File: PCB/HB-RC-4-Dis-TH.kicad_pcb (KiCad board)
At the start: 2 copper layers, 53 x 53 mm, 41 parts, among them J1 FTDI, J2 SHT31, J3 eInk, J4 ISP, J5 Power, Q1 IRLML6346TRBPF, SW1 T1, SW2 T2, SW3 T3, SW4 T4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

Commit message: update pcb
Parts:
- SHT31: renamed from J2; footprint Connector_PinHeader_2.00mm:PinHeader_1x04_P2.00mm_Vertical -> Connector_PinHeader_2.54mm:PinHeader_1x04_P2.54mm_Vertical
- moved SHT31 2.38 mm to (31.8, 81.3)
- moved J3 1.20 mm to (58.3, 106.5)
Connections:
- J3 pad : (no net) -> GND
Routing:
- net /RESET: track 65.1 -> 120.5 mm, vias 0 -> 3
- net Net-(C7-Pad1): track 25.5 -> 78.6 mm
- net /MOSI: track 91.1 -> 60.4 mm, vias 1 -> 3
- net GND: track 242.0 -> 264.6 mm, vias 10 -> 40
- net Net-(SW3-Pad1): track 72.4 -> 91.4 mm
- net +3V3: track 171.5 -> 189.9 mm
- net Net-(SW2-Pad1): track 24.8 -> 40.6 mm
- net /RST: track 39.7 -> 24.4 mm
- net Net-(C2-Pad1): track 22.0 -> 36.0 mm, vias 2 -> 0
- net /RX: track 66.1 -> 80.1 mm
- net /BUSY: track 41.8 -> 27.9 mm
- net /MISO: track 56.8 -> 44.2 mm
- net /DC: track 35.1 -> 25.0 mm, vias 3 -> 1
- net Net-(R1-Pad1): track 42.2 -> 51.6 mm
- net Net-(SW5-Pad1): track 74.0 -> 64.7 mm
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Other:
- outline, holes or cut-outs redrawn

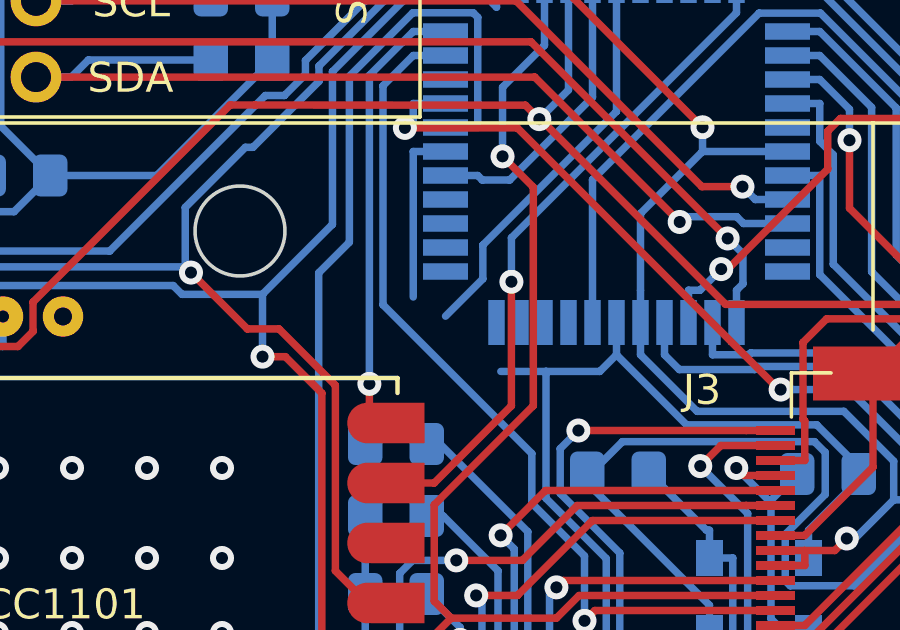
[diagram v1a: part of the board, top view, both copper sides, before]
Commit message: add via
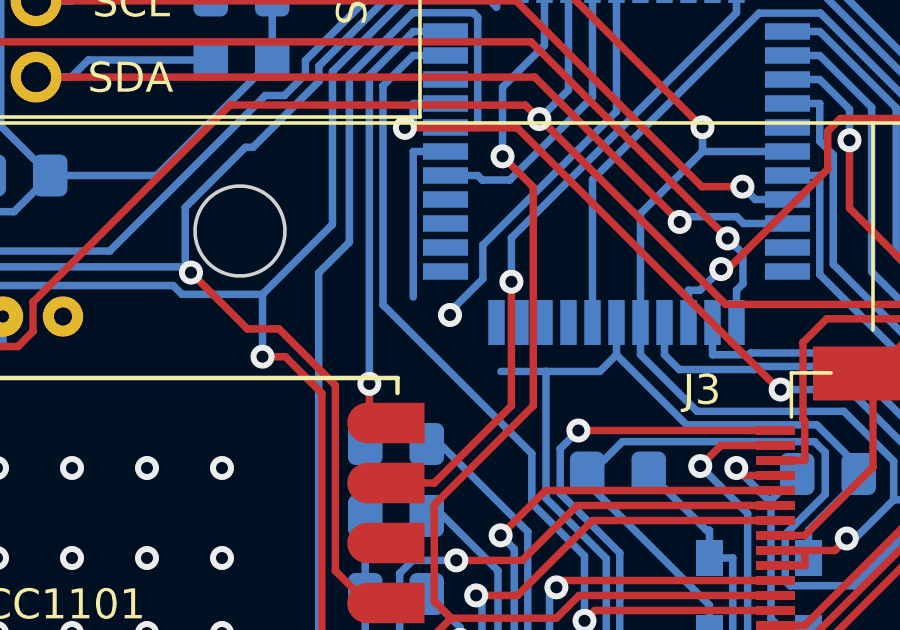
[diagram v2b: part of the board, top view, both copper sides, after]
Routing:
- net GND: vias 40 -> 41
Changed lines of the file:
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@@
     (thickness 1.6)
     (drawings 57)
-    (tracks 698)
+    (tracks 699)
     (zones 0)
     (modules 41)
@@
   (segment (start 44.3747 91.45) (end 44.3747 96.3) (width 0.25) (layer B.Cu) (net 3))
   (segment (start 45.45 91.45) (end 44.3747 91.45) (width 0.25) (layer B.Cu) (net 3))
+  (via (at 45.6 96.9) (size 0.8) (drill 0.4) (layers F.Cu B.Cu) (net 3))
   (segment (start 50.35 97.15) (end 50.35 92.39) (width 0.25) (layer B.Cu) (net 4))
   (segment (start 50.35 92.39) (end 55.9024 86.8376) (width 0.25) (layer B.Cu) (net 4))

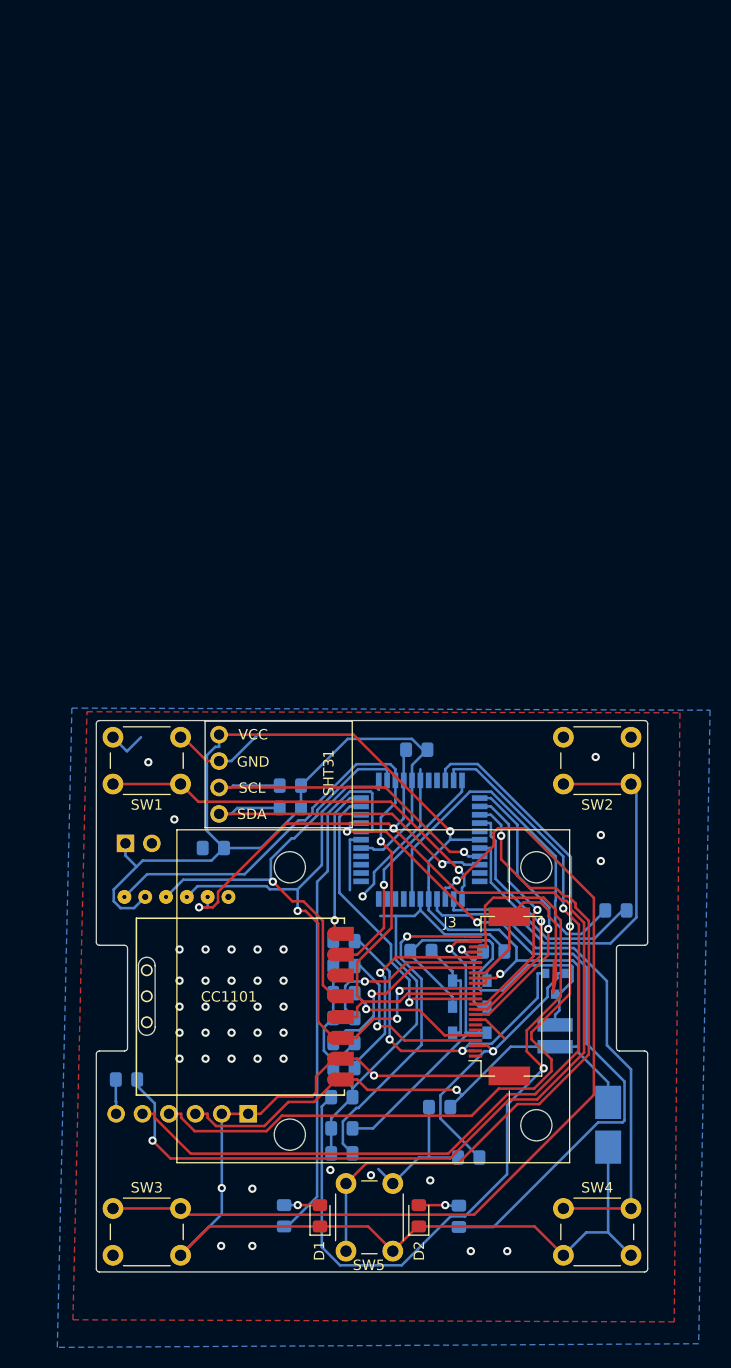
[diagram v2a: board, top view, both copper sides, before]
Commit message: update pcb v1.1 (added decoupling capacitors)
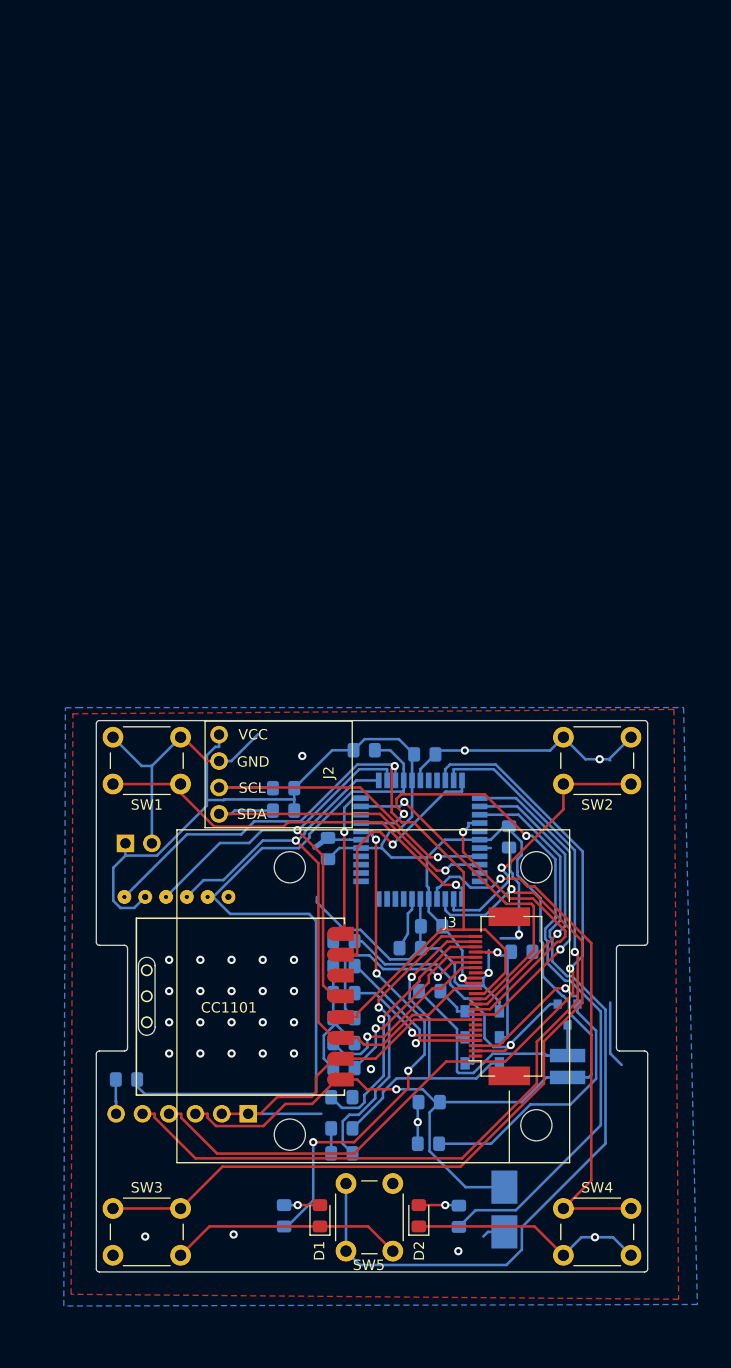
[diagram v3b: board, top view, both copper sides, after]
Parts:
- added C15: 100n, Capacitor_SMD:C_0805_2012Metric_Pad1.15x1.40mm_HandSolder, B.Cu at (51.6, 83.2)
- added C16: 100n, Capacitor_SMD:C_0805_2012Metric_Pad1.15x1.40mm_HandSolder, B.Cu at (59.7, 91.2)
- added C17: 100n, Capacitor_SMD:C_0805_2012Metric_Pad1.15x1.40mm_HandSolder, B.Cu at (52.2, 99.8)
- moved C2 20.1 mm to (50.2, 101.9)
- moved C18 12.9 mm to (59.2, 127.0)
- moved C14 11.0 mm to (42.3, 92.3), turned to 90 degrees
- moved R3 5.05 mm to (45.8, 82.8), turned to 0 degrees
- moved R8 4.10 mm to (51.9, 120.7)
- moved C11 3.94 mm to (52.0, 106.0)
- moved D3 3.18 mm to (57.1, 108.0)
- moved D4 3.18 mm to (57.1, 110.5)
- moved D5 3.18 mm to (57.1, 113.0)
- moved L1 3.18 mm to (65.3, 113.2)
- moved Q1 3.18 mm to (65.3, 108.2)
- moved C12 2.70 mm to (60.9, 102.2)
- moved C3 1.11 mm to (52.0, 116.7)
- moved R4 0.70 mm to (38.0, 86.5)
- moved R5 0.70 mm to (38.0, 88.7)
- renumbered C15 to C18, SHT31 to J2
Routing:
- net Net-(C7-Pad1): track 78.6 -> 24.8 mm
- net GND: track 264.6 -> 215.2 mm, vias 41 -> 31
- net /RESET: track 120.5 -> 74.8 mm, vias 3 -> 0
- net Net-(C2-Pad1): track 36.0 -> 5.15 mm
- net Net-(SW2-Pad1): track 40.6 -> 26.3 mm, vias 0 -> 1
- net Net-(SW5-Pad1): track 64.7 -> 78.0 mm, vias 1 -> 0
- net Net-(C11-Pad1): track 37.1 -> 24.5 mm
- net Net-(SW3-Pad1): track 91.4 -> 79.1 mm
- net /RESE: track 27.0 -> 38.8 mm
- net +3V3: track 189.9 -> 181.1 mm, vias 3 -> 2
- net /SCK: track 71.8 -> 79.0 mm
- net /PREVGL: track 28.4 -> 35.2 mm
- net /RST: track 24.4 -> 29.1 mm
- net /DC: track 25.0 -> 28.7 mm
- net /CC1101_GDO0: track 23.1 -> 26.9 mm
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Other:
- board text added: "HB-RC-4-Dis-TH (c) 2020 jp112sdl V1.1"
- board text removed: "HB-RC-4-Dis-TH (c) 2020 jp112sdl V1.0"

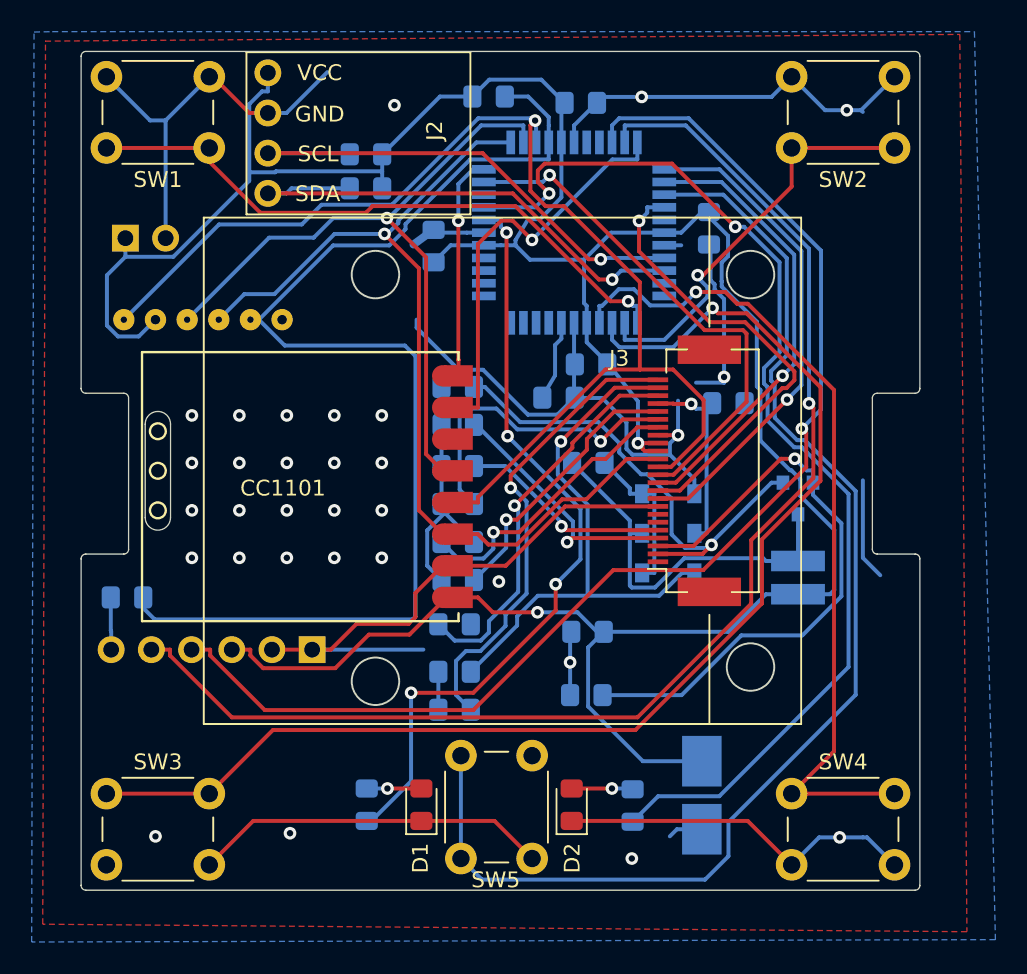
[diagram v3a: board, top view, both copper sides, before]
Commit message: shrink pcb to 51x51
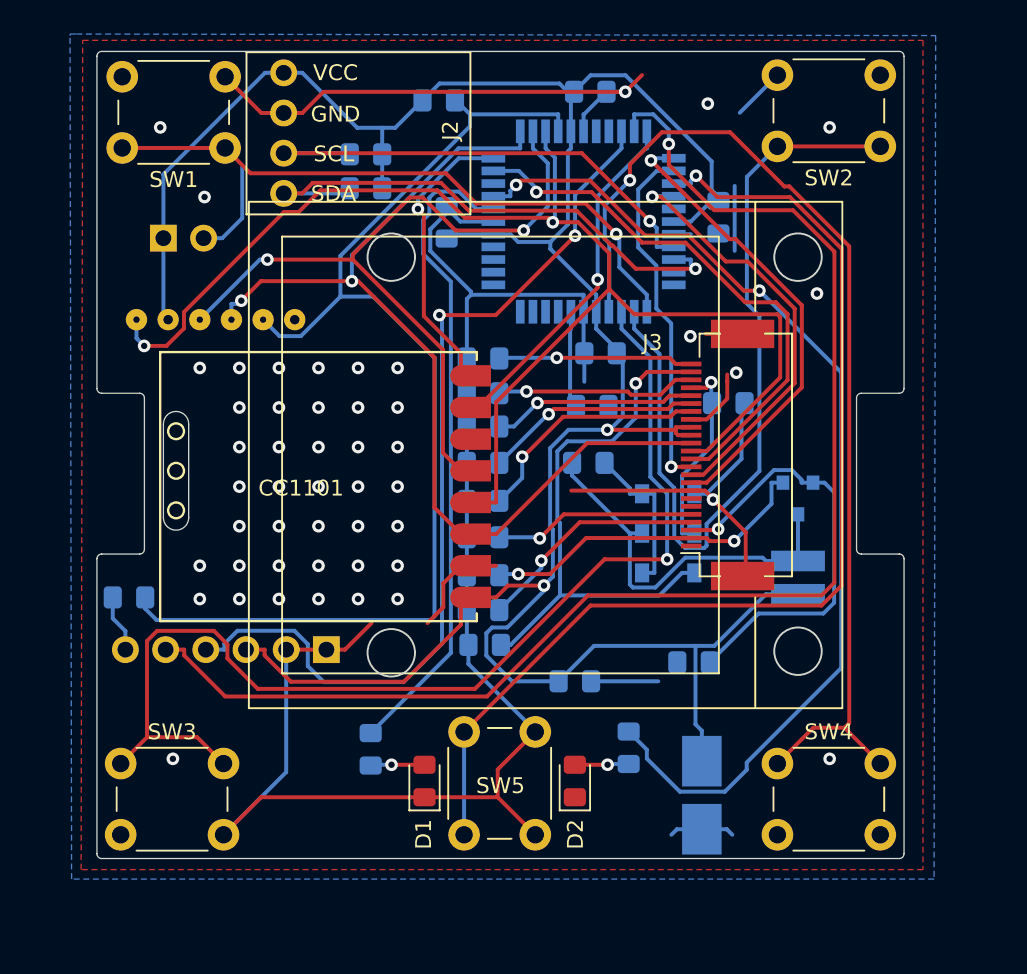
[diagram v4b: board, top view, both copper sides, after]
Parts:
- D1: value LED gn -> LED rt
- D2: value LED rt -> gn
- R1, R2: value 1k -> 330
- moved C8 22.3 mm to (45.4, 99.4)
- moved C7 14.7 mm to (45.4, 101.6), turned to 180 degrees
- moved R6 12.0 mm to (45.4, 113.1)
- moved C9 11.8 mm to (45.4, 115.3)
- moved C6 9.83 mm to (45.4, 103.7)
- moved R8 7.09 mm to (58.7, 118.6)
- moved C10 4.78 mm to (45.4, 110.7)
- moved R2 3.66 mm to (54.6, 124.0), turned to 270 degrees
- moved R1 3.51 mm to (38.3, 124.1), turned to 270 degrees
- moved C3 3.23 mm to (51.2, 119.8), turned to 0 degrees
- moved R3 3.16 mm to (42.6, 83.1)
- moved C4 3.05 mm to (45.4, 108.4), turned to 180 degrees
- moved C5 3.05 mm to (45.4, 106.0)
- moved C13 2.55 mm to (45.5, 117.5)
- moved J5 2.40 mm to (25.2, 91.8)
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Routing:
- net GND: track 215.2 -> 187.3 mm, vias 31 -> 49
- net Net-(SW2-Pad1): track 26.3 -> 51.9 mm, vias 1 -> 0
- net /RX: track 79.2 -> 58.1 mm, vias 1 -> 2
- net Net-(C8-Pad1): track 29.9 -> 12.3 mm
- net Net-(SW4-Pad1): track 52.8 -> 66.7 mm
- net Net-(C7-Pad1): track 24.8 -> 12.7 mm
- net /RESE: track 38.8 -> 27.8 mm
- net Net-(SW3-Pad1): track 79.1 -> 69.4 mm
- net Net-(SW5-Pad1): track 78.0 -> 68.3 mm, vias 0 -> 1
- net /GDR: track 30.8 -> 21.3 mm, vias 1 -> 2
- net /SCK: track 79.0 -> 87.4 mm, vias 1 -> 2
- net +3V3: track 181.1 -> 172.7 mm
- net Net-(R1-Pad1): track 49.2 -> 41.5 mm, vias 4 -> 0
- net Net-(C5-Pad1): track 20.2 -> 13.7 mm
- net /DC: track 28.7 -> 22.4 mm
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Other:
- board size 53 x 53 mm -> 51 x 51 mm
- board text added: "HB-RC-4-Dis-TH (c) 2020 jp112sdl V1.2"
- board text removed: "HB-RC-4-Dis-TH (c) 2020 jp112sdl V1.1"

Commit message: update
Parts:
- moved J4 2.05 mm to (33.5, 94.9)
- moved U2 2.00 mm to (46.5, 114.0)
- moved J5 1.43 mm to (24.6, 90.5)
- moved C14 0.23 mm to (43.3, 90.8)
- moved C13 0.10 mm to (45.4, 117.5)
- moved C6 0.10 mm to (45.4, 103.8)
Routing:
- net +3V3: track 172.7 -> 204.8 mm, vias 2 -> 5
- net Net-(SW3-Pad1): track 69.4 -> 101.4 mm
- net /RX: track 58.1 -> 87.2 mm, vias 2 -> 1
- net Net-(SW2-Pad1): track 51.9 -> 24.1 mm
- net GND: track 187.3 -> 207.6 mm, vias 49 -> 53
- net Net-(SW4-Pad1): track 66.7 -> 46.8 mm, vias 1 -> 0
- net /GDR: track 21.3 -> 41.1 mm, vias 2 -> 1
- net Net-(SW5-Pad1): track 68.3 -> 81.1 mm, vias 1 -> 0
- net Net-(C11-Pad1): track 24.5 -> 35.3 mm
- net /SCK: track 87.4 -> 76.7 mm
- net /DC: track 22.4 -> 31.1 mm
- net /PREVGL: track 35.1 -> 28.7 mm
- net Net-(C10-Pad1): track 12.8 -> 19.0 mm
- net Net-(R1-Pad1): track 41.5 -> 46.3 mm
- net Net-(R2-Pad1): track 65.1 -> 69.8 mm, vias 2 -> 0
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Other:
- outline, holes or cut-outs redrawn
- board text added: "-"

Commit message: update 1.2
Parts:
- moved L1 1.73 mm to (65.3, 111.5)
- moved Q1 0.57 mm to (65.3, 107.7)
- moved C18 0.20 mm to (59.2, 126.8)
- renumbered J2 to SHT31
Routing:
- net GND: track 207.6 -> 178.4 mm, vias 53 -> 62
- net Net-(C11-Pad1): track 35.3 -> 33.9 mm
- net /RESE: track 26.2 -> 26.8 mm
- net +3V3: track 204.8 -> 204.2 mm
- net /GDR: track 41.1 -> 40.6 mm

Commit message: update
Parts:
- added C19: 10/6, Capacitor_SMD:C_0805_2012Metric_Pad1.15x1.40mm_HandSolder, B.Cu at (33.5, 123.4)
- added C20: 10/6, Capacitor_SMD:C_0805_2012Metric_Pad1.15x1.40mm_HandSolder, B.Cu at (69.7, 119.5)
- added D6: LED bl, LED_SMD:LED_0805_2012Metric_Pad1.15x1.40mm_HandSolder, F.Cu at (47.1, 81.5)
- added J6: Batt, Connector_PinHeader_2.54mm:PinHeader_1x02_P2.54mm_Vertical, B.Cu at (33.5, 126.3)
- added JP1: SolderJumper_3_Open, Jumper:SolderJumper-3_P1.3mm_Open_RoundedPad1.0x1.5mm, B.Cu at (54.6, 121.9)
- added R10: 100k, Resistor_SMD:R_0805_2012Metric_Pad1.15x1.40mm_HandSolder, B.Cu at (60.3, 94.6)
- added R11: 1k, Resistor_SMD:R_0805_2012Metric_Pad1.15x1.40mm_HandSolder, B.Cu at (60.5, 84.7)
- added R12: 240, Resistor_SMD:R_0805_2012Metric_Pad1.15x1.40mm_HandSolder, B.Cu at (58.2, 81.4)
- added R7: 2k2, Resistor_SMD:R_0805_2012Metric_Pad1.15x1.40mm_HandSolder, B.Cu at (38.2, 129.5)
- added R9: 470k, Resistor_SMD:R_0805_2012Metric_Pad1.15x1.40mm_HandSolder, B.Cu at (64.2, 122.2)
- added U3: MCP1703T-3302E/CB, Package_TO_SOT_SMD:SOT-23, B.Cu at (69.6, 116.2)
- added U4: MCP73831T-2ACI/OT, Package_TO_SOT_SMD:SOT-23-5, B.Cu at (38.1, 126.2)
- U1: value ATmega644PA-AU -> ATmega1284P-AU
- moved J5 46.6 mm to (54.6, 126.2), turned to 180 degrees
- moved R2 7.46 mm to (52.3, 116.9), turned to 180 degrees
- moved C3 6.48 mm to (52.2, 113.4)
- moved R1 2.91 mm to (40.6, 122.4), turned to 0 degrees
- moved C1 1.18 mm to (24.2, 114.5)
- moved J1 0.40 mm to (35.9, 117.8)
- moved C11 0.25 mm to (52.3, 106.0)
- renumbered SHT31 to J2
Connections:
- J3 pad : GND -> (no net)
- J5 pad 1: +3V3 -> Net-(J5-Pad1)
- U1 pad 21: Net-(U1-Pad21) -> /B_ACTIVATION
- U1 pad 22: Net-(U1-Pad22) -> /B_CHARGING
- U1 pad 37: Net-(U1-Pad37) -> /B_MEASURE
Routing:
- net Net-(D6-Pad2): track 0.00 -> 96.2 mm, vias 0 -> 1
- net Net-(R11-Pad1): track 0.00 -> 77.8 mm, vias 0 -> 2
- net +BATT: track 0.00 -> 52.7 mm, vias 0 -> 1
- net /B_MEASURE: track 0.00 -> 45.1 mm, vias 0 -> 2
- net GND: track 178.4 -> 134.4 mm, vias 62 -> 40
- net Net-(R2-Pad1): track 69.8 -> 34.4 mm
- net /TX: track 89.0 -> 54.9 mm, vias 1 -> 2
- net Net-(SW3-Pad1): track 101.4 -> 74.2 mm
- net /GDR: track 40.6 -> 21.2 mm, vias 1 -> 2
- net Net-(D6-Pad1): track 0.00 -> 14.4 mm, vias 0 -> 1
- net Net-(SW5-Pad1): track 81.1 -> 67.0 mm, vias 0 -> 1
- net /B_CHARGING: track 0.00 -> 13.8 mm
- net Net-(C11-Pad1): track 33.9 -> 22.8 mm, vias 0 -> 2
- net /RESET: track 69.7 -> 80.2 mm
- net /PREVGL: track 28.7 -> 37.5 mm
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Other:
- board text added: "Batt"
- board text added: "HB-RC-4-Dis-TH (c) 2020 jp112sdl"
- board text added: "LiPo"
- board text removed: "-"
- board text removed: "HB-RC-4-Dis-TH (c) 2020 jp112sdl V1.2"

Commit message: update
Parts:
- removed J2: SHT31, Connector_PinHeader_2.54mm:PinHeader_1x04_P2.54mm_Vertical
- added R13: 100k, Resistor_SMD:R_0805_2012Metric_Pad1.15x1.40mm_HandSolder, B.Cu at (57.1, 30.6)
- added SHT31: SHT31, Connector_PinHeader_2.54mm:PinHeader_1x04_P2.54mm_Vertical, F.Cu at (25.6, 14.8)
- added U5: PC357, Package_SO:SO-4_4.4x3.6mm_P2.54mm, F.Cu at (48.8, 19.1)
- C19, C20: value 10/6 -> 10/10
- R11: value 1k -> 680
- moved R4 67.2 mm to (29.2, 19.9)
- moved R12 67.2 mm to (49.0, 14.8)
- moved LiPo 67.1 mm to (26.3, 59.6)
- moved C2 67.0 mm to (45.1, 35.8)
- moved C3 67.0 mm to (45.0, 46.8)
- moved C4 67.0 mm to (38.2, 41.8)
- moved C8 67.0 mm to (38.2, 32.8)
- moved J4 67.0 mm to (26.3, 28.3)
- moved JP1 67.0 mm to (47.4, 55.3)
- moved R1 67.0 mm to (33.5, 55.8)
- moved R2 67.0 mm to (45.1, 50.3)
- moved U4 67.0 mm to (30.9, 59.6)
- moved C10 67.0 mm to (38.2, 44.1)
- moved C12 67.0 mm to (53.7, 35.7)
- moved C13 67.0 mm to (38.2, 50.9)
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- renumbered J6 to LiPo
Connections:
- R11 pad 2: /B_CHARGING -> Net-(R11-Pad2)
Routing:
- net GND: track 134.4 -> 220.2 mm, vias 40 -> 48
- net /RX: track 83.1 -> 54.2 mm, vias 1 -> 2
- net /TX: track 54.9 -> 80.4 mm, vias 2 -> 1
- net Net-(D6-Pad2): track 96.2 -> 76.6 mm
- net Net-(SW5-Pad1): track 67.0 -> 79.9 mm, vias 1 -> 0
- net /RESET: track 80.2 -> 70.5 mm, vias 0 -> 2
- net Net-(D6-Pad1): track 14.4 -> 5.80 mm
- net /MOSI: track 63.6 -> 57.8 mm
- net /PREVGL: track 37.5 -> 42.2 mm, vias 1 -> 2
- net Net-(SW3-Pad1): track 74.2 -> 69.5 mm
- net /SCK: track 81.2 -> 76.8 mm
- net /B_CHARGING: track 13.8 -> 17.9 mm, vias 0 -> 1
- net /DISP_CS: track 38.0 -> 34.1 mm
- net /B_MEASURE: track 45.1 -> 48.3 mm
- net Net-(R11-Pad1): track 77.8 -> 80.6 mm
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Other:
- board text added: "V2.0"
